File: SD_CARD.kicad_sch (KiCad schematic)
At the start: 6 parts, among them J2 Micro_SD_Card

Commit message: dfvdfv
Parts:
- R5, R6, R7, R8: value 10k -> 4.7k
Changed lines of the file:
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@@
 			)
 		)
-		(property "Value" "10k"
+		(property "Value" "4.7k"
 			(at 143.764 82.296 0)
 			(effects
@@
 			)
 		)
-		(property "Value" "10k"
+		(property "Value" "4.7k"
 			(at 155.448 82.296 0)
 			(effects
@@
 			)
 		)
-		(property "Value" "10k"
+		(property "Value" "4.7k"
 			(at 163.068 82.296 0)
 			(effects
@@
 			)
 		)
-		(property "Value" "10k"
+		(property "Value" "4.7k"
 			(at 131.064 82.296 0)
 			(effects

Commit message: changes to schematic and PCB
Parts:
- added J11, J12, J13, J14: Conn_01x03_Pin, Connector_PinHeader_2.54mm:PinHeader_1x03_P2.54mm_Vertical, symbol Connector:Conn_01x03_Pin
- C5: footprint (none) -> Capacitor_SMD:C_0805_2012Metric
- J2: footprint (none) -> Connector_Card:microSD_HC_Molex_104031-0811
- R5, R6, R7, R8: footprint (none) -> Resistor_SMD:R_0805_2012Metric
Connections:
- net SPI_CLK renamed SPI_Clk_SD
- net SPI_Clk_SD: now also J13.1 (Pin_1)
- net SPI_CS renamed SPI_Cs_SD
- net SPI_Cs_SD: now also J11.1 (Pin_1)
- net SPI_PICO renamed SPI_Mosi_SD
- net SPI_Mosi_SD: now also J12.1 (Pin_1)
- net SPI_POCI renamed SPI_Miso_SD
- net SPI_Miso_SD: now also J14.1 (Pin_1)
- new net SPI_Clk: J13.2 (Pin_2)
- new net SPI_Clk_Break: J13.3 (Pin_3)
- new net SPI_Cs: J11.2 (Pin_2)
- new net SPI_Cs_Break: J11.3 (Pin_3)
- new net SPI_Miso: J14.2 (Pin_2)
- new net SPI_Miso_Break: J14.3 (Pin_3)
- new net SPI_Mosi: J12.2 (Pin_2)
- new net SPI_Mosi_Break: J12.3 (Pin_3)

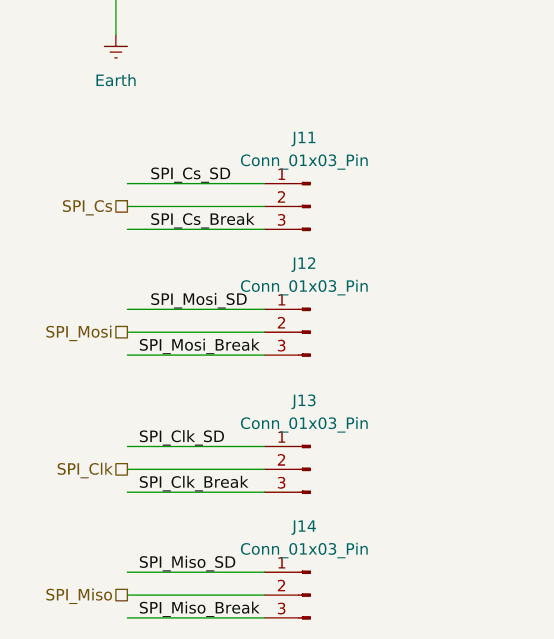
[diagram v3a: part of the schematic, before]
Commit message: changed schematics
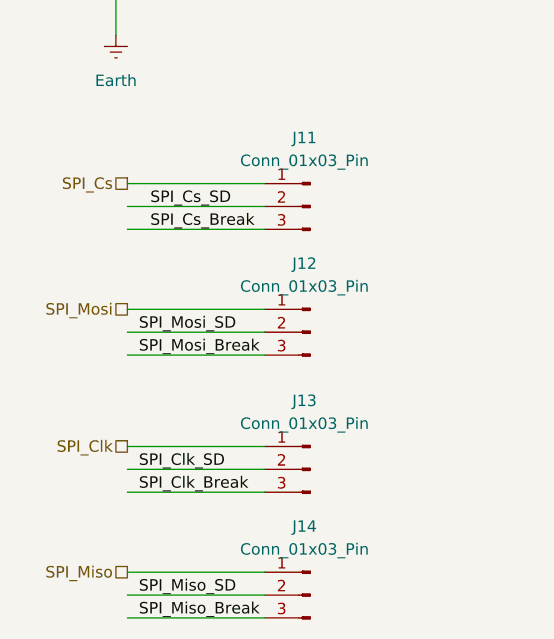
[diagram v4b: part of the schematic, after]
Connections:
- net SPI_Clk: now also J13.1 (Pin_1); no longer J13.2 (Pin_2)
- net SPI_Clk_SD: now also J13.2 (Pin_2); no longer J13.1 (Pin_1)
- net SPI_Cs: now also J11.1 (Pin_1); no longer J11.2 (Pin_2)
- net SPI_Cs_SD: now also J11.2 (Pin_2); no longer J11.1 (Pin_1)
- net SPI_Miso: now also J14.1 (Pin_1); no longer J14.2 (Pin_2)
- net SPI_Miso_SD: now also J14.2 (Pin_2); no longer J14.1 (Pin_1)
- net SPI_Mosi: now also J12.1 (Pin_1); no longer J12.2 (Pin_2)
- net SPI_Mosi_SD: now also J12.2 (Pin_2); no longer J12.1 (Pin_1)
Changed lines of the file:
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@@
+	(wire
+		(pts
+			(xy 160.02 96.52) (xy 163.83 96.52)
+		)
+		(stroke
+			(width 0)
+			(type default)
+		)
+	)
+	(wire
+		(pts
+			(xy 99.06 101.6) (xy 163.83 101.6)
+		)
+		(stroke
+			(width 0)
+			(type default)
+		)
+	)
+	(wire
+		(pts
+			(xy 85.09 93.98) (xy 85.09 96.52)
+		)
+		(stroke
+			(width 0)
+			(type default)
+		)
+	)
+	(wire
+		(pts
+			(xy 140.97 72.39) (xy 152.4 72.39)
+		)
+		(stroke
+			(width 0)
+			(type default)
+		)
+	)
+	(wire
+		(pts
+			(xy 86.36 162.56) (xy 101.6 162.56)
+		)
+		(stroke
+			(width 0)
+			(type default)
+		)
+	)
+	(wire
+		(pts
+			(xy 85.09 93.98) (xy 85.09 72.39)
+		)
+		(stroke
+			(width 0)
+			(type default)
+		)
+	)
+	(wire
+		(pts
+			(xy 86.36 173.99) (xy 101.6 173.99)
+		)
+		(stroke
+			(width 0)
+			(type default)
+		)
+	)
+	(wire
+		(pts
+			(xy 160.02 86.36) (xy 160.02 96.52)
+		)
+		(stroke
+			(width 0)
+			(type default)
+		)
+	)
 	(wire
 		(pts
@@
 	(wire
 		(pts
-			(xy 86.36 173.99) (xy 101.6 173.99)
-		)
-		(stroke
-			(width 0)
-			(type default)
-		)
-	)
-	(wire
-		(pts
-			(xy 160.02 96.52) (xy 163.83 96.52)
-		)
-		(stroke
-			(width 0)
-			(type default)
-		)
-	)
-	(wire
-		(pts
-			(xy 99.06 101.6) (xy 163.83 101.6)
-		)
-		(stroke
-			(width 0)
-			(type default)
-		)
-	)
-	(wire
-		(pts
-			(xy 85.09 93.98) (xy 85.09 96.52)
-		)
-		(stroke
-			(width 0)
-			(type default)
-		)
-	)
-	(wire
-		(pts
-			(xy 140.97 72.39) (xy 152.4 72.39)
-		)
-		(stroke
-			(width 0)
-			(type default)
-		)
-	)
-	(wire
-		(pts
-			(xy 85.09 93.98) (xy 85.09 72.39)
-		)
-		(stroke
-			(width 0)
-			(type default)
-		)
-	)
-	(wire
-		(pts
-			(xy 160.02 86.36) (xy 160.02 96.52)
-		)
-		(stroke
-			(width 0)
-			(type default)
-		)
-	)
-	(wire
-		(pts
 			(xy 160.02 72.39) (xy 152.4 72.39)
 		)
@@
 	(wire
 		(pts
+			(xy 86.36 176.53) (xy 101.6 176.53)
+		)
+		(stroke
+			(width 0)
+			(type default)
+		)
+	)
+	(wire
+		(pts
 			(xy 128.27 72.39) (xy 140.97 72.39)
 		)
@@
 	(wire
 		(pts
+			(xy 128.27 78.74) (xy 128.27 72.39)
+		)
+		(stroke
+			(width 0)
+			(type default)
+		)
+	)
+	(wire
+		(pts
+			(xy 85.09 106.68) (xy 163.83 106.68)
+		)
+		(stroke
+			(width 0)
+			(type default)
+		)
+	)
+	(wire
+		(pts
+			(xy 152.4 99.06) (xy 163.83 99.06)
+		)
+		(stroke
+			(width 0)
+			(type default)
+		)
+	)
+	(wire
+		(pts
+			(xy 152.4 86.36) (xy 152.4 99.06)
+		)
+		(stroke
+			(width 0)
+			(type default)
+		)
+	)
+	(wire
+		(pts
 			(xy 86.36 144.78) (xy 101.6 144.78)
 		)
@@
 	(wire
 		(pts
-			(xy 128.27 78.74) (xy 128.27 72.39)
-		)
-		(stroke
-			(width 0)
-			(type default)
-		)
-	)
-	(wire
-		(pts
-			(xy 86.36 176.53) (xy 101.6 176.53)
+			(xy 128.27 86.36) (xy 128.27 109.22)
 		)
 		(stroke
@@
 	(wire
 		(pts
-			(xy 85.09 106.68) (xy 163.83 106.68)
-		)
-		(stroke
-			(width 0)
-			(type default)
-		)
-	)
-	(wire
-		(pts
-			(xy 152.4 99.06) (xy 163.83 99.06)
-		)
-		(stroke
-			(width 0)
-			(type default)
-		)
-	)
-	(wire
-		(pts
-			(xy 152.4 86.36) (xy 152.4 99.06)
-		)
-		(stroke
-			(width 0)
-			(type default)
-		)
-	)
-	(wire
-		(pts
-			(xy 86.36 162.56) (xy 101.6 162.56)
-		)
-		(stroke
-			(width 0)
-			(type default)
-		)
-	)
-	(wire
-		(pts
-			(xy 128.27 86.36) (xy 128.27 109.22)
-		)
-		(stroke
-			(width 0)
-			(type default)
-		)
-	)
-	(wire
-		(pts
 			(xy 85.09 72.39) (xy 85.09 69.85)
 		)
@@
 	(wire
 		(pts
+			(xy 128.27 109.22) (xy 114.3 109.22)
+		)
+		(stroke
+			(width 0)
+			(type default)
+		)
+	)
+	(wire
+		(pts
 			(xy 86.36 160.02) (xy 101.6 160.02)
-		)
-		(stroke
-			(width 0)
-			(type default)
-		)
-	)
-	(wire
-		(pts
-			(xy 128.27 109.22) (xy 114.3 109.22)
 		)
 		(stroke
@@
 	)
 	(label "SPI_Cs_SD"
-		(at 88.9 130.81 0)
+		(at 88.9 133.35 0)
 		(fields_autoplaced yes)
 		(effects
@@
 	)
 	(label "SPI_Miso_SD"
-		(at 87.63 173.99 0)
+		(at 87.63 176.53 0)
 		(fields_autoplaced yes)
 		(effects
@@
 	)
 	(label "SPI_Mosi_SD"
-		(at 88.9 144.78 0)
+		(at 87.63 147.32 0)
 		(fields_autoplaced yes)
 		(effects
@@
 	)
 	(label "SPI_Clk_SD"
-		(at 87.63 160.02 0)
+		(at 87.63 162.56 0)
 		(fields_autoplaced yes)
 		(effects
@@
 	(hierarchical_label "SPI_Cs"
 		(shape passive)
-		(at 86.36 133.35 180)
+		(at 86.36 130.81 180)
 		(fields_autoplaced yes)
 		(effects
@@
 	(hierarchical_label "SPI_Mosi"
 		(shape passive)
-		(at 86.36 147.32 180)
+		(at 86.36 144.78 180)
 		(fields_autoplaced yes)
 		(effects
@@
 	(hierarchical_label "SPI_Miso"
 		(shape passive)
-		(at 86.36 176.53 180)
+		(at 86.36 173.99 180)
 		(fields_autoplaced yes)
 		(effects
@@
 	(hierarchical_label "SPI_Clk"
 		(shape passive)
-		(at 86.36 162.56 180)
-		(fields_autoplaced yes)
-		(effects
+		(at 86.36 160.02 180)
+		(fields_autoplaced yes)
+		(effects
